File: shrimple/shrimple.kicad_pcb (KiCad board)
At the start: 2 copper layers, 249.2 x 105.6 mm, 116 parts, among them U3 Sparkfun_Pro_Micro

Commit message: moved MCU, rerouted
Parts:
- removed the G*** at (208.0, 42.4)
- G***: moved to B.Cu
- R1: moved to F.Cu
- moved G*** 18.3 mm to (217.5, 41.8), turned to 180 degrees
- moved U3 1.84 mm to (245.2, 48.9)
- moved R1 0.10 mm to (164.0, 37.1)
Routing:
- net ROW4: track 332.9 -> 335.3 mm
- net ROW3: track 296.1 -> 298.5 mm
- net COL11: track 113.4 -> 115.4 mm
- net ROW2: track 263.4 -> 265.0 mm
- net COL4: track 229.5 -> 227.9 mm
- net COL2: track 268.6 -> 267.1 mm
- net RGBDATA: track 96.2 -> 94.7 mm
- net COL5: track 181.8 -> 180.3 mm
- net COL0: track 312.5 -> 311.0 mm
- net +5V: track 108.4 -> 106.8 mm
- net COL3: track 226.7 -> 225.1 mm
- net COL1: track 292.5 -> 291.0 mm
- net ROW1: track 224.9 -> 226.2 mm
- net COL10: track 86.1 -> 85.2 mm
- net ROW0: track 356.8 -> 357.6 mm
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
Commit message: changed mcu to aliexpress pro micro
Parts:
- LED1: value VAL** -> WS2812B
- U3: value Sparkfun_Pro_Micro -> Pro Micro RP2040; footprint arduino:Sparkfun_Pro_Micro -> rp2040:pro_micro_rp2040
- moved U3 20.2 mm to (244.1, 28.8), turned to -90 degrees
- moved G*** 6.71 mm to (223.5, 38.8)
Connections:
- U3 pad 1: COL11 -> ROW2
- U3 pad 10: COL4 -> unconnected-(U3-GP10-Pad10)
- U3 pad 11: COL5 -> unconnected-(U3-GP11-Pad11)
- U3 pad 2: ROW3 -> ROW1
- U3 pad 20: RGBDATA -> COL8
- U3 pad 21: unconnected-(U3-VCC-Pad21) -> COL6
- U3 pad 22: unconnected-(U3-RST-Pad22) -> COL9
- U3 pad 23: GND -> COL7
- U3 pad 3: GND -> ROW0
- U3 pad 4: GND -> COL5
- U3 pad 5: ROW4 -> COL4
- U3 pad 6: COL0 -> COL3
- U3 pad 7: COL1 -> COL2
- U3 pad 8: COL2 -> COL1
- U3 pad 9: COL3 -> COL0
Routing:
- net ROW2: track 265.0 -> 319.6 mm
- net ROW1: track 226.2 -> 264.5 mm
- net ROW4: track 335.3 -> 316.5 mm
- net COL0: track 311.0 -> 295.4 mm
- net ROW0: track 357.6 -> 372.8 mm
- net COL10: track 85.2 -> 96.9 mm
- net COL5: track 180.3 -> 192.0 mm
- net COL6: track 177.7 -> 166.8 mm
- net COL1: track 291.0 -> 280.8 mm
- net ROW3: track 298.5 -> 289.1 mm
- net COL4: track 227.9 -> 234.2 mm
- net COL9: track 107.9 -> 113.4 mm
- net COL7: track 131.8 -> 126.4 mm
- net COL2: track 267.1 -> 262.4 mm
- net COL11: track 115.4 -> 117.2 mm
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
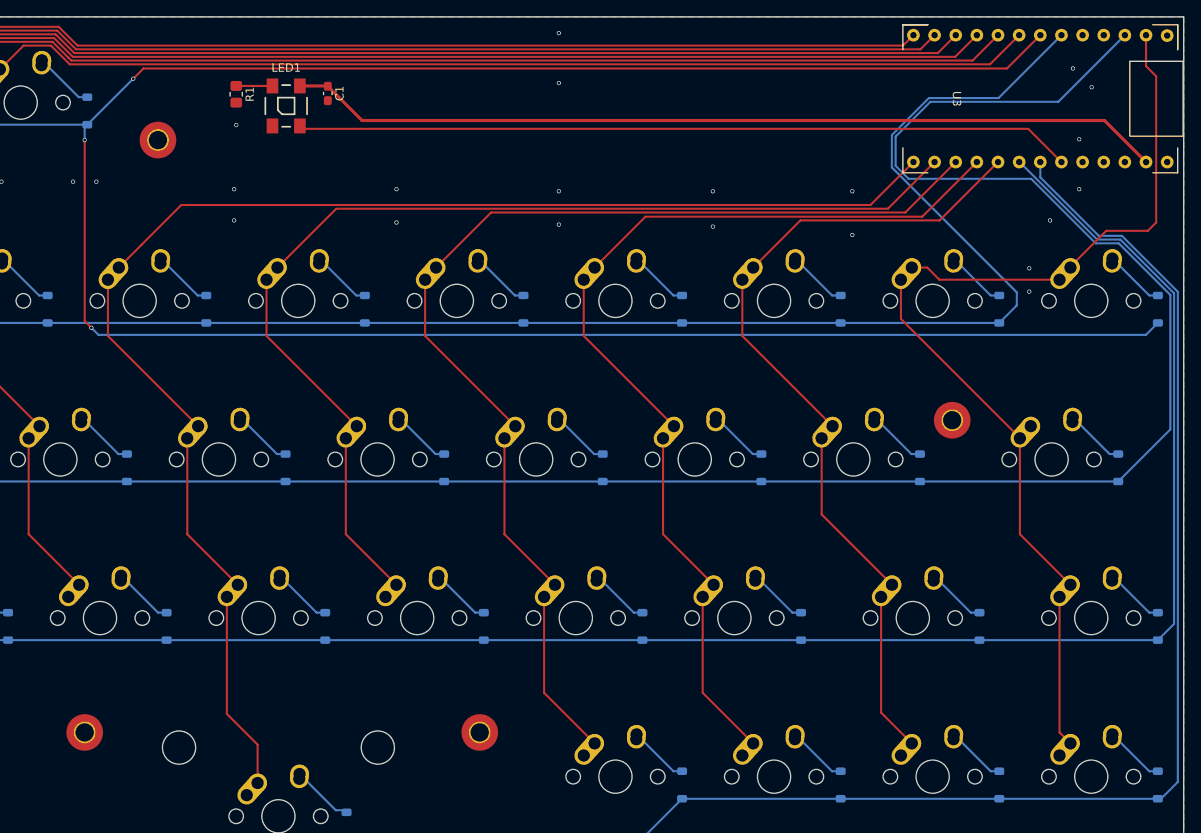
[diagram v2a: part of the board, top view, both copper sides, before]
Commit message: flipped mcu and rerouted
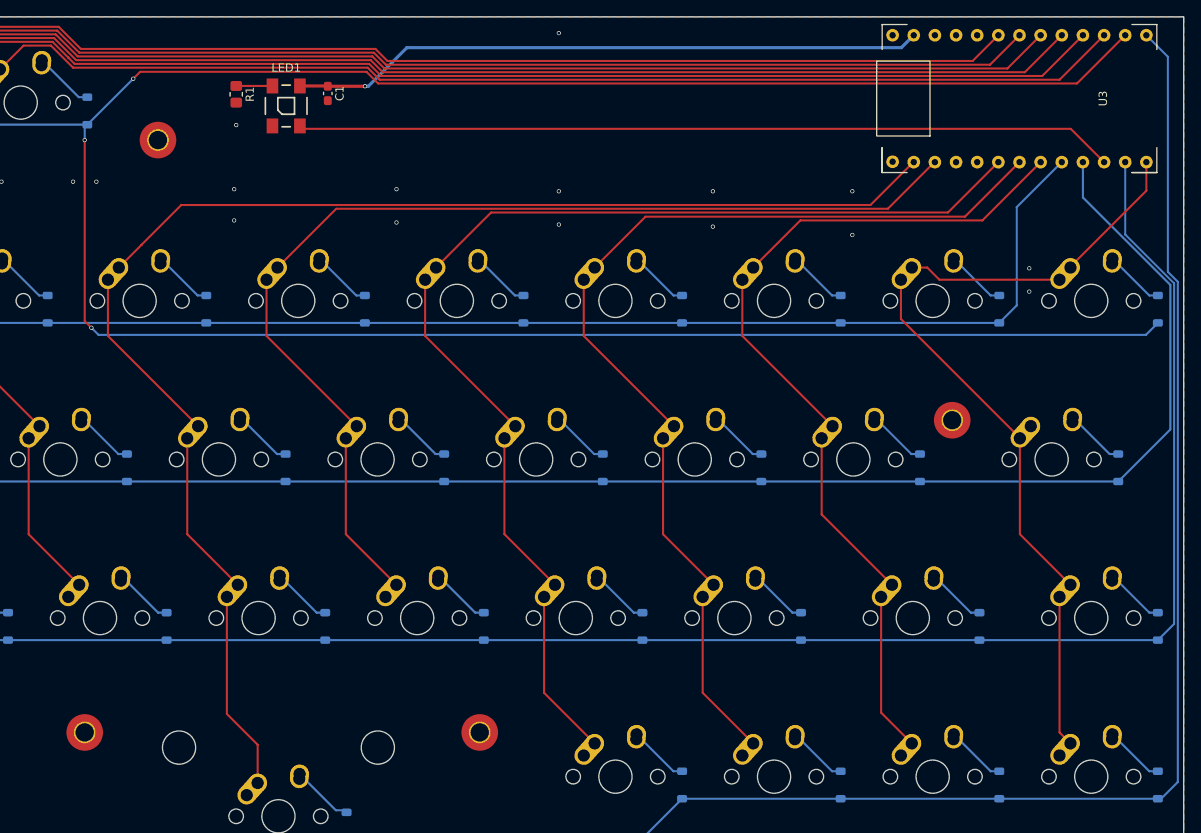
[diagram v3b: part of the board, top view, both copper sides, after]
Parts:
- moved U3 35.3 mm to (274.6, 46.5), turned to 90 degrees
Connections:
- U3 pad 0: COL11 -> COL6
- U3 pad 1: ROW2 -> COL7
- U3 pad 2: ROW1 -> COL8
- U3 pad 20: COL8 -> COL5
- U3 pad 21: COL6 -> ROW4
- U3 pad 22: COL9 -> COL4
- U3 pad 23: COL7 -> ROW0
- U3 pad 26: COL10 -> COL3
- U3 pad 27: ROW3 -> COL2
- U3 pad 28: ROW4 -> COL1
- U3 pad 29: RGBDATA -> COL0
- U3 pad 3: ROW0 -> COL9
- U3 pad 4: COL5 -> COL10
- U3 pad 5: COL4 -> ROW1
- U3 pad 6: COL3 -> ROW2
- U3 pad 7: COL2 -> RGBDATA
- U3 pad 8: COL1 -> ROW3
- U3 pad 9: COL0 -> COL11
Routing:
- net ROW2: track 319.6 -> 264.4 mm
- net ROW1: track 264.5 -> 232.0 mm
- net +5V: track 105.4 -> 76.3 mm, vias 0 -> 1
- net COL11: track 117.2 -> 98.0 mm
- net COL4: track 234.2 -> 246.0 mm
- net COL2: track 262.4 -> 274.1 mm
- net COL5: track 192.0 -> 203.7 mm
- net COL3: track 225.9 -> 237.6 mm
- net COL1: track 280.8 -> 292.6 mm
- net COL0: track 295.4 -> 307.1 mm
- net ROW0: track 372.8 -> 384.2 mm
- net ROW4: track 316.5 -> 324.8 mm
- net ROW3: track 289.1 -> 282.1 mm
- net COL9: track 113.4 -> 118.6 mm
- net RGBDATA: track 93.3 -> 98.4 mm
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
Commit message: Squashed commit of the following:
commit 0917563cd294cf20495b95da51ce8923af6e95fb
Author: anchovie-codes <littlebrother.free@gmail.com>
Date:   Fri Feb 14 11:46:37 2025 -0500

    updated firmware gpio and layout

commit 7b5bbbd23beed7ff01c20b44607d9c6e08a5b151
Author: anchovie-codes <littlebrother.free@gmail.com>
Date:   Thu Feb 13 21:50:05 2025 -0500

    Update gerbers.zip

commit e1b025b53f2bea44497d56d99e089700163ef0fc
Author: anchovie-codes <littlebrother.free@gmail.com>
Date:   Thu Feb 13 21:41:48 2025 -0500

    moved mounting hole, updated gerbers

commit b07354e94ad3d0d744c50304922b6d94077aa1cf
Author: anchovie-codes <littlebrother.free@gmail.com>
Date:   Thu Feb 13 21:30:55 2025 -0500

    fixed layout, added level shifter, made gerbers
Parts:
- added C2: C_Small, Capacitor_SMD:C_0603_1608Metric_Pad1.08x0.95mm_HandSolder, F.Cu at (177.9, 37.0)
- added U2: SN74LV1T34DCK, Package_TO_SOT_SMD:SOT-353_SC-70-5, F.Cu at (179.5, 41.3)
- MX1, MX10, MX11, MX12, MX13, MX14, MX15, MX16, MX17, MX18, MX19, MX2, MX21, MX22, MX23, MX24, MX25, MX26, MX27, MX28, MX29, MX3, MX30, MX33, MX34, MX35, MX36, MX37, MX38, MX39, MX4, MX40, MX41, MX43, MX45, MX49, MX5, MX50, MX51, MX52, MX6, MX7, MX8, MX9: footprint hybrids:MX-1U-NoLED -> MX_V2:MX-Solderable-1U
- MX20: footprint hybrids:MX-1.5U-NoLED -> MX_V2:MX-Solderable-1.25U
- MX31: footprint hybrids:MX-1.5U-NoLED -> MX_V2:MX-Solderable-1.75U
- MX32: footprint hybrids:MX-1.75U-NoLED -> MX_V2:MX-Solderable-1.75U
- MX42, MX44, MX46: footprint hybrids:MX-1.25U-NoLED -> MX_V2:MX-Solderable-1.25U
- MX47: footprint hybrids:MX-2.25U-ReversedStabilizers-NoLED -> MX_V2:MX-Solderable-2.25U-ReversedStabilizers
- MX48: footprint hybrids:MX-2.75U-ReversedStabilizers-NoLED -> MX_V2:MX-Solderable-2.75U-ReversedStabilizers
- moved D26 4.76 mm to (165.2, 82.0)
- moved D28 4.76 mm to (203.3, 82.0)
- moved MX26 4.76 mm to (157.2, 81.0)
- moved MX28 4.76 mm to (195.3, 81.0)
- moved D21 4.76 mm to (69.9, 82.0)
- moved D23 4.76 mm to (108.0, 82.0)
- moved MX23 4.76 mm to (100.0, 81.0)
- moved MX24 4.76 mm to (119.1, 81.0)
- moved MX21 4.76 mm to (61.9, 81.0)
- moved D22 4.76 mm to (89.0, 82.0)
- moved D24 4.76 mm to (127.1, 82.0)
- moved D25 4.76 mm to (146.1, 82.0)
- moved D27 4.76 mm to (184.2, 82.0)
- moved D29 4.76 mm to (222.3, 82.0)
- moved D30 4.76 mm to (241.4, 82.0)
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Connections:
- LED1 pad 4: RGBDATA -> LED_OUT
- U3 pad 7: RGBDATA -> LED_IN
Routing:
- net LED_IN: track 0.00 -> 98.9 mm
- net RGBDATA: track 98.4 -> 0.00 mm
- net LED_OUT: track 0.00 -> 8.96 mm
- net COL2: track 274.1 -> 281.4 mm
- net COL4: track 246.0 -> 253.0 mm
- net COL1: track 292.6 -> 298.8 mm
- net COL0: track 307.1 -> 313.2 mm
- net COL5: track 203.7 -> 209.6 mm
- net COL11: track 98.0 -> 103.7 mm
- net COL8: track 135.1 -> 140.4 mm
- net +5V: track 76.3 -> 81.5 mm
- net COL3: track 237.6 -> 242.6 mm
- net COL9: track 118.6 -> 123.6 mm
- net COL10: track 102.1 -> 106.7 mm
- net COL6: track 166.8 -> 171.4 mm
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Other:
- board text added: "designed by anchovie https://anchovie.art"
- board text removed: "design by anchovie https://anchovie.art"
